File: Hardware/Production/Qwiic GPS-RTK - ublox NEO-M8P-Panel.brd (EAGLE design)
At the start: 95.5 x 94.2 mm, 411 parts, among them J10 U.FL, J13 U.FL, J14 PTH, J17 U.FL, J20 PTH, J23 U.FL, J3 PTH, J7 PTH, U1 NEO-M8P, U2 3.3V, U3 NEO-M8P, U4 3.3V, U5 NEO-M8P, U6 3.3V, U7 NEO-M8P, U8 3.3V

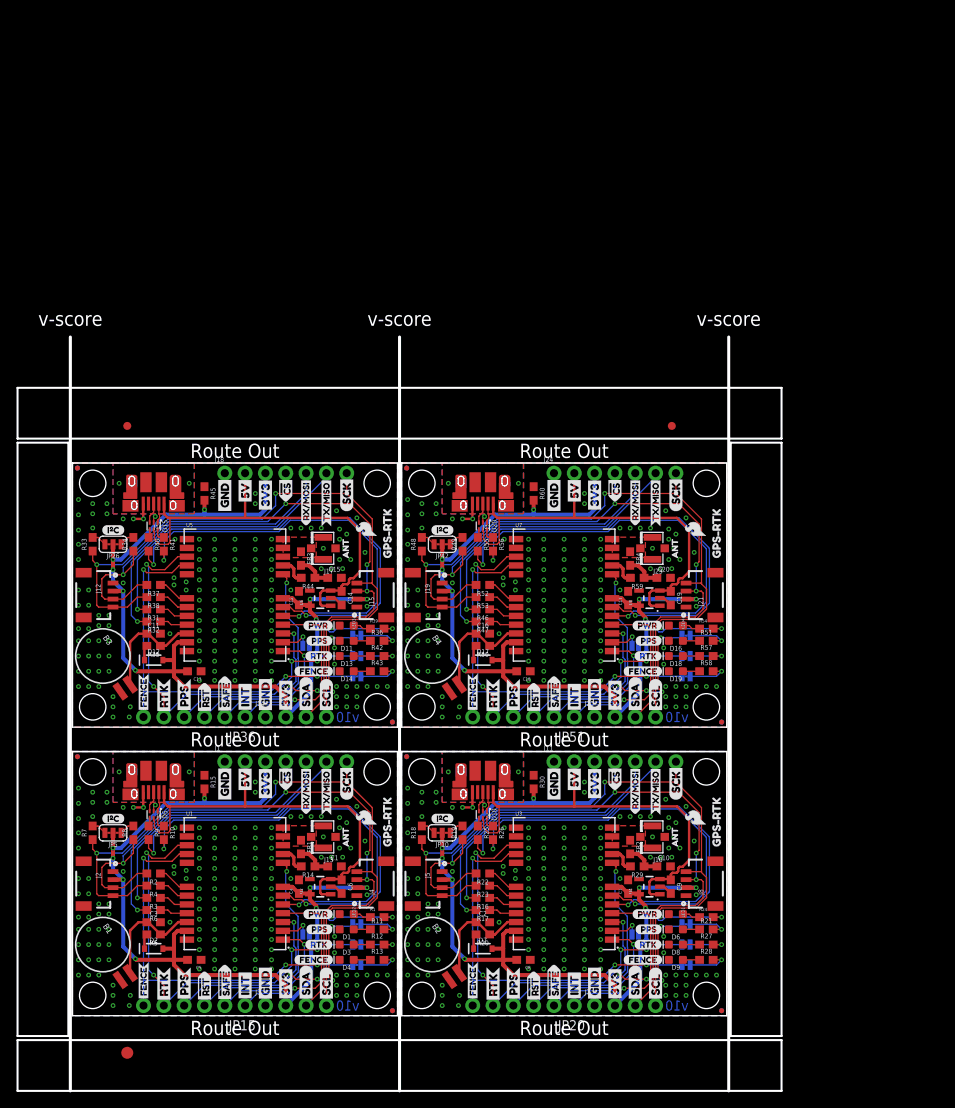
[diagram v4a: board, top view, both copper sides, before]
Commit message: Adds Panel for v20
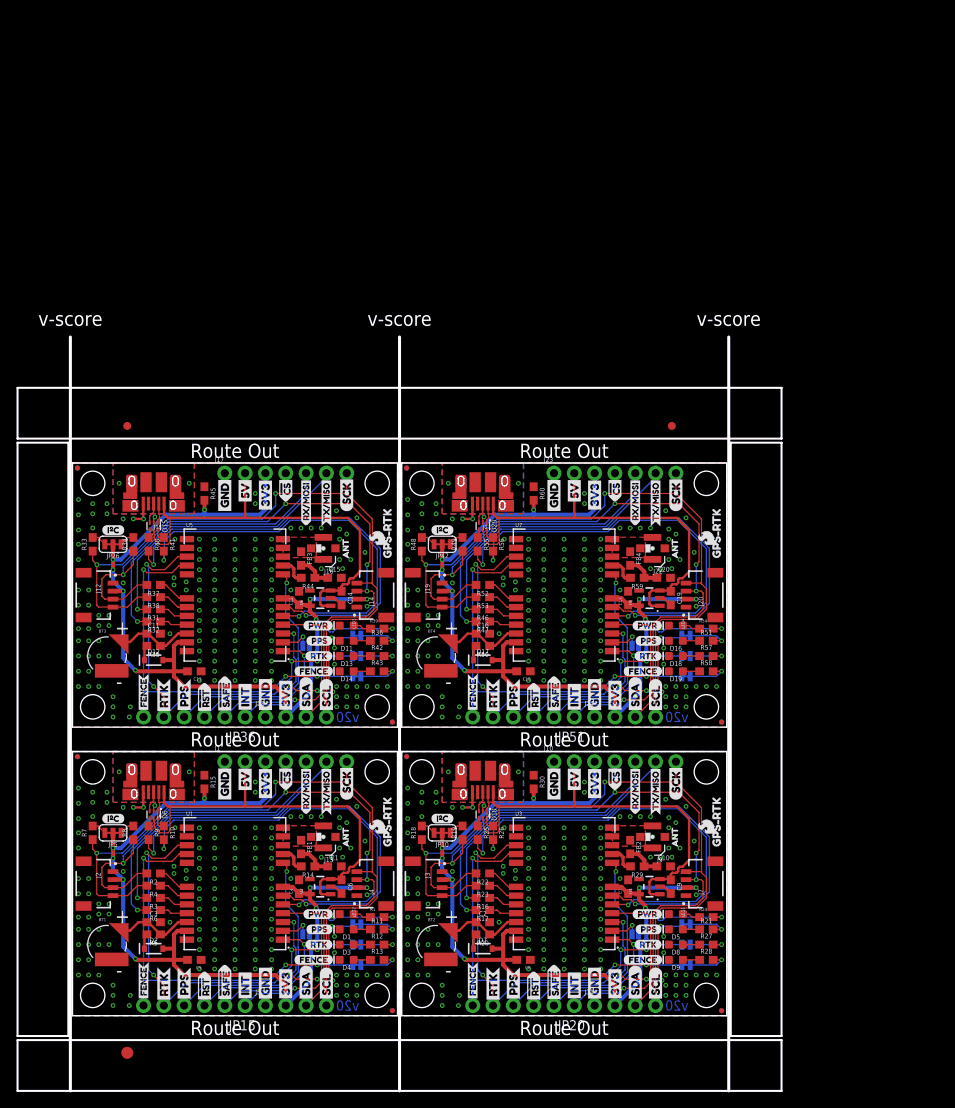
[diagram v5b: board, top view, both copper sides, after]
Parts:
- removed B1, B2, B3, B4: 6.8MM_COIN_CELL, SparkFun-Batteries:BATTCON-6.8MM
- added BT1, BT2, BT3, BT4: ML414H_IV01E_BATTERY, SparkFun-Batteries:ML414H_IV01E
- D10, D15, D20: device funbit:SOT886 -> SparkFun-IC-Power:SOT886
- D5: value PRTR5V0U2F -> Yellow; device funbit:SOT886 -> SparkFun-LED:LED-0603
- D6: value Yellow -> PRTR5V0U2F; device SparkFun-LED:LED-0603 -> SparkFun-IC-Power:SOT886
- J10, J17, J23: value U.FL -> (none); device SparkFun-Connectors:U.FL -> SparkFun-Connectors:1X07_NO_SILK
- J11, J18, J24: device SparkFun-Connectors:1X07_NO_SILK -> SparkFun-Connectors:1X04_NO_SILK
- J12, J19, J2, J4: value (none) -> Qwiic Right Angle; device SparkFun-Connectors:1X04_1MM_RA -> SparkFun-Connectors:JST04_1MM_RA
- J14, J20, J3, J7: value PTH -> Qwiic Right Angle; device SparkX:1X04_NO_SILK -> SparkFun-Connectors:JST04_1MM_RA
- J15, J21, J8: device SparkFun-Connectors:1X04_1MM_RA -> SparkFun-Connectors:USB-MICROB-PTH-MILL
- J16, J22, J9: value (none) -> U.FL; device SparkFun-Connectors:USB-MICROB-PTH-MILL -> SparkFun-Connectors:U.FL
- J5: device SparkFun-Connectors:1X04_1MM_RA -> SparkFun-Connectors:1X04_NO_SILK
- JP1, JP11, JP18, JP19, JP2, JP27, JP3, JP34, JP35, JP43, JP49, JP50: value (none) -> JUMPER-SMT_2_NC_TRACE_SILK
- JP10, JP26, JP42, JP5: value (none) -> JUMPER-SMT_3_2-NC_TRACE_SILK
- JP101, JP14, JP16, JP22, JP23, JP30, JP31, JP32, JP37, JP38, JP41, JP46, JP47, JP6, JP7, JP91: value STAND-OFF -> STAND-OFFTIGHT; device SparkFun:STAND-OFF -> SparkFun-Hardware:STAND-OFF-TIGHT
- JP12, JP13, JP21, JP24, JP25, JP28, JP29, JP39, JP40, JP44, JP45, JP61, JP71, JP8, JP81, JP9: device SparkFun:MICRO-FIDUCIAL -> SparkFun-Aesthetics:FIDUCIAL-MICRO
- JP17, JP33, JP4, JP48: value (none) -> JUMPER-SMT_2_NO_SILK
- U1, U3, U5, U7: device NEO-M8P:NEO-M8P -> SparkFun-GPS:NEO-M8P
- moved D5 66.8 mm to (75.4, 10.8), turned to 180 degrees
- moved D6 66.8 mm to (10.2, 25.1), turned to 270 degrees
- moved J11 30.9 mm to (65.3, 1.27)
- moved J24 30.9 mm to (65.3, 37.3)
- moved J18 30.9 mm to (24.1, 37.3)
- moved J15 27.9 mm to (10.2, 64.0), turned to 180 degrees
- moved J8 27.9 mm to (51.3, 27.9), turned to 180 degrees
- moved J21 27.9 mm to (51.3, 64.0), turned to 180 degrees
- moved J3 26.8 mm to (46.2, 16.5), turned to 270 degrees
- moved J5 26.8 mm to (24.1, 1.27), turned to 0 degrees
- moved J16 21.9 mm to (31.4, 58.4)
- moved J22 21.9 mm to (72.5, 58.4)
- moved J9 21.9 mm to (72.5, 22.4)
- moved J14 19.1 mm to (35.6, 52.6), turned to 90 degrees
- moved J20 19.0 mm to (76.7, 52.6), turned to 90 degrees
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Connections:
- net 3.3V: now also J5.2; no longer J3.2
- net 3.3V1: now also J10.3, J11.2, J3.2; no longer J11.3, J5.2, J8.2
- net 3.3V2: now also J17.3, J18.2; no longer J15.2, J18.3
- net 3.3V3: now also J23.3, J24.2; no longer J21.2, J24.3
- net 5V: now also D6.5; no longer D5.5
- net 5V1: now also J10.2, J8.VBUS; no longer J11.2, J9.VBUS
- net 5V2: now also J15.VBUS, J17.2; no longer J16.VBUS, J18.2
- net 5V3: now also J21.VBUS, J23.2; no longer J22.VBUS, J24.2
- net BACKUP: now also BT1.+; no longer B1.+
- net BACKUP1: now also BT2.+; no longer B2.+
- net BACKUP2: now also BT3.+; no longer B3.+
- net BACKUP3: now also BT4.+; no longer B4.+
- net D+: now also D6.4; no longer D5.4
- net D-: now also D6.6; no longer D5.6
- net GND: now also BT1.-, D6.2, J5.1; no longer B1.-, D5.2, J3.1
- net GND1: now also BT2.-, D5.C, J3.1, J8.GND, J9.1, J9.2; no longer B2.-, D6.C, J10.2, J5.1, J8.1, J9.GND
- net GND2: now also BT3.-, J15.GND, J16.1, J16.2; no longer B3.-, J15.1, J16.GND, J17.2
- net GND3: now also BT4.-, J21.GND, J22.1, J22.2; no longer B4.-, J21.1, J22.GND, J23.2
- net GPS_ANT2: now also J9.FEED; no longer J10.FEED
- net GPS_ANT3: now also J16.FEED; no longer J17.FEED
- net GPS_ANT4: now also J22.FEED; no longer J23.FEED
- net N$16: now also D5.A; no longer D6.A
- net RXI/MOSI1: now also J10.5; no longer J11.5
- net RXI/MOSI2: now also J17.5; no longer J18.5
- net RXI/MOSI3: now also J23.5; no longer J24.5
- net SCL/SCK: now also J5.4; no longer J3.4
- net SCL/SCK1: now also J10.7, J11.4, J3.4; no longer J11.7, J5.4, J8.4
- net SCL/SCK2: now also J17.7, J18.4; no longer J15.4, J18.7
- net SCL/SCK3: now also J23.7, J24.4; no longer J21.4, J24.7
- net SDA/!CS: now also J5.3; no longer J3.3
- net SDA/!CS1: now also J10.4, J11.3, J3.3; no longer J11.4, J5.3, J8.3
- net SDA/!CS2: now also J17.4, J18.3; no longer J15.3, J18.4
- net SDA/!CS3: now also J23.4, J24.3; no longer J21.3, J24.4
- net SHLD1: now also J8.SHIELD, J8.SHIELD10, J8.SHIELD2, J8.SHIELD3, J8.SHIELD4, J8.SHIELD5, J8.SHIELD6, J8.SHIELD7, J8.SHIELD8, J8.SHIELD9; no longer J9.SHIELD, J9.SHIELD10, J9.SHIELD2, J9.SHIELD3, J9.SHIELD4, J9.SHIELD5, J9.SHIELD6, J9.SHIELD7, J9.SHIELD8, J9.SHIELD9
- net SHLD2: now also J15.SHIELD, J15.SHIELD10, J15.SHIELD2, J15.SHIELD3, J15.SHIELD4, J15.SHIELD5, J15.SHIELD6, J15.SHIELD7, J15.SHIELD8, J15.SHIELD9; no longer J16.SHIELD, J16.SHIELD10, J16.SHIELD2, J16.SHIELD3, J16.SHIELD4, J16.SHIELD5, J16.SHIELD6, J16.SHIELD7, J16.SHIELD8, J16.SHIELD9
- net SHLD3: now also J21.SHIELD, J21.SHIELD10, J21.SHIELD2, J21.SHIELD3, J21.SHIELD4, J21.SHIELD5, J21.SHIELD6, J21.SHIELD7, J21.SHIELD8, J21.SHIELD9; no longer J22.SHIELD, J22.SHIELD10, J22.SHIELD2, J22.SHIELD3, J22.SHIELD4, J22.SHIELD5, J22.SHIELD6, J22.SHIELD7, J22.SHIELD8, J22.SHIELD9
- net TXO/MISO1: now also J10.6; no longer J11.6
- net TXO/MISO2: now also J17.6; no longer J18.6
- net TXO/MISO3: now also J23.6; no longer J24.6
- net USB_D+: now also D6.3; no longer D5.3
- net USB_D+1: now also J8.D+; no longer J9.D+
- net USB_D+2: now also J15.D+; no longer J16.D+
- net USB_D+3: now also J21.D+; no longer J22.D+
- net USB_D-: now also D6.1; no longer D5.1
- net USB_D-1: now also J8.D-; no longer J9.D-
- net USB_D-2: now also J15.D-; no longer J16.D-
- net USB_D-3: now also J21.D-; no longer J22.D-
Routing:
- net BACKUP1: track 14.1 -> 9.80 mm
- net BACKUP: track 14.1 -> 9.80 mm
- net BACKUP2: track 14.1 -> 9.80 mm
- net BACKUP3: track 14.1 -> 9.80 mm
- net GND1: track 5.71 -> 5.61 mm, vias 161 -> 158
- net GND: track 5.71 -> 5.61 mm, vias 161 -> 158
- net GND3: track 5.71 -> 5.61 mm, vias 161 -> 158
- net GND2: track 5.71 -> 5.61 mm, vias 161 -> 158
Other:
- board text added: "+"
- board text added: "-"
- board text added: "v20"
- board text removed: "v10"

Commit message: Repanelizes for a larger panel 2x3 instead of 2x2
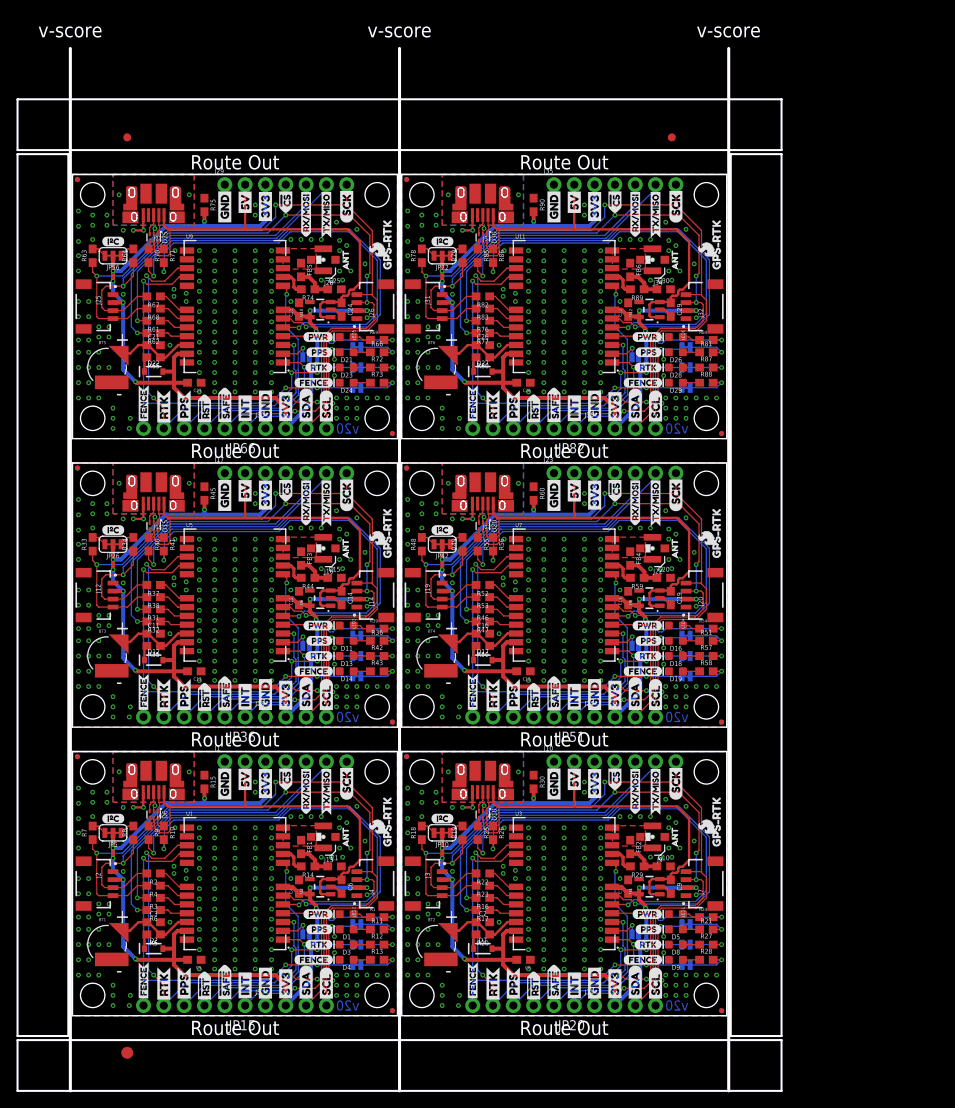
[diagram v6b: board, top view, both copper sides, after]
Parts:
- added BT5, BT6: ML414H_IV01E_BATTERY, SparkFun-Batteries:ML414H_IV01E
- added C21, C22, C24, C26, C27, C29: 1.0uF, SparkFun-Capacitors:0603
- added C23, C28: 0.1uF, SparkFun-Capacitors:0603
- added C25, C30: 47pF, SparkFun-Capacitors:0603
- added D21, D26: Yellow, SparkFun-LED:LED-0603
- added D22, D27: 0.5A/40V/420mV, SparkFun-DiscreteSemi:SOD-323
- added D23, D28: GREEN, SparkFun-LED:LED-0603
- added D24, D29: BLUE, SparkFun-LED:LED-0603
- added D25, D30: PRTR5V0U2F, SparkFun-IC-Power:SOT886
- added FB5, FB6: 30Ω/1.8A, SparkFun-Coils:0603
- added J25, J26, J31, J32: Qwiic Right Angle, SparkFun-Connectors:JST04_1MM_RA
- added J27, J33: (no value), SparkFun-Connectors:USB-MICROB-PTH-MILL
- added J28, J34: U.FL, SparkFun-Connectors:U.FL
- added J29, J35: (no value), SparkFun-Connectors:1X07_NO_SILK
- added J30, J36: (no value), SparkFun-Connectors:1X04_NO_SILK
- added JP52, JP53, JP60, JP62, JP67, JP68, JP76, JP77: STAND-OFFTIGHT, SparkFun-Hardware:STAND-OFF-TIGHT
- added JP54, JP55, JP58, JP59, JP69, JP70, JP74, JP75: FIDUCIALUFIDUCIAL, SparkFun-Aesthetics:FIDUCIAL-MICRO
- added JP56, JP72: JUMPER-SMT_3_2-NC_TRACE_SILK, SparkFun-Jumpers:SMT-JUMPER_3_2-NC_TRACE_SILK
- added JP57, JP64, JP65, JP73, JP79, JP80: JUMPER-SMT_2_NC_TRACE_SILK, SparkFun-Jumpers:SMT-JUMPER_2_NC_TRACE_SILK
- added JP63, JP78: JUMPER-SMT_2_NO_SILK, SparkFun-Jumpers:SMT-JUMPER_2_NO_SILK
- added JP66, JP82: (no value), SparkFun-Connectors:1X06_NO_SILK
- added LED5, LED6: RED, SparkFun-LED:LED-0603
- added LOGO10, LOGO12: SFE_LOGO_NAME_FLAME.1_INCH, SparkFun-Aesthetics:SFE_LOGO_NAME_FLAME_.1
- added LOGO11, LOGO9: OSHW-LOGOMINI, SparkFun-Aesthetics:OSHW-LOGO-MINI
- added R61, R62, R67, R68, R76, R77, R82, R83: 33, SparkFun-Resistors:0603
- added R63, R64, R78, R79: 2.2k, SparkFun-Resistors:0603
- added R65, R66, R69, R72, R73, R80, R81, R84, R87, R88: 1k, SparkFun-Resistors:0603
- added R70, R71, R85, R86: 27, SparkFun-Resistors:0603
- added R74, R89: 10, SparkFun-Resistors:0603
- added R75, R90: 100k, SparkFun-Resistors:0603
- added U$201, U$203, U$251, U$253: (no value), Labels:SDA-[)
- added U$202, U$204, U$252, U$254: (no value), Labels:SCL-[)
- added U$205, U$206, U$228, U$229, U$255, U$256, U$278, U$279: (no value), Labels:3V3-04
- added U$207, U$208, U$230, U$231, U$257, U$258, U$280, U$281: (no value), Labels:GND-04
- added U$209, U$259: (no value), Labels:I_SUPER2_C-()-03
- added U$210, U$211, U$260, U$261: (no value), buzzard_labels (5):INT8
- added U$212, U$262: (no value), buzzard_labels (5):U#BLOX3
- added U$213, U$263: (no value), Labels:QWIIC-LOGO-MEDIUM
- added U$214, U$215, U$264, U$265: (no value), buzzard_labels (7):#RST3
- added U$216, U$217, U$266, U$267: (no value), buzzard_labels (7):#SAFE1
- added U$218, U$219, U$268, U$269: (no value), buzzard_labels (7):PPS5
- added U$220, U$270: (no value), buzzard_labels (33):PPS0
- added U$221, U$271: (no value), buzzard_labels:FENCE2
- added U$222, U$272: (no value), buzzard_labels:JP20
- added U$223, U$273: (no value), buzzard_labels:RTK1
- added U$224, U$225, U$274, U$275: (no value), buzzard_labels (1):FENCE0
- added U$226, U$227, U$276, U$277: (no value), buzzard_labels (1):RTK1
- added U$232, U$282: (no value), buzzard_labels (3):GPS#RTK0
- added U$233, U$283: (no value), buzzard_labels (5):JP10
- added U$234, U$284: (no value), buzzard_labels (5):JP32
- added U$235, U$285: (no value), buzzard_labels (6):DSEL0
- added U$236, U$286: (no value), buzzard_labels (7):NEO#M8P3
- added U$237, U$287: (no value), buzzard_labels (8):GPS#RTK1
- added U$238, U$288: (no value), buzzard_labels (9):ANT0
- added U$239, U$289: (no value), Labels:PWR-()-03
- added U$240, U$241, U$290, U$291: (no value), Labels:5V
- added U$242, U$243, U$292, U$293: (no value), Labels:CS#-<]
- added U$244, U$245, U$294, U$295: (no value), Labels:SCK-(]-04
- added U$246, U$296: (no value), SparkFun-Aesthetics:SFE_LOGO_FLAME_.1
- added U$247, U$297: (no value), buzzard_labels (36):RX#MOSI2
- added U$248, U$298: (no value), buzzard_labels (36):RX#MOSI3
- added U$249, U$299: (no value), buzzard_labels (36):TX#MISO0
- added U$250, U$300: (no value), buzzard_labels (36):TX#MISO1
- added U10, U12: 3.3V, SparkFun-IC-Power:SOT23-5
- added U11, U9: NEO-M8P, SparkFun-GPS:NEO-M8P
- moved E$1 36.1 mm to (6.86, 109.8)
- moved E$2 36.1 mm to (74.9, 109.8)
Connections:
- new net !RESET4: JP66.3, U9.8
- new net !RESET5: JP82.3, U11.8
- new net !SAFE4: JP66.2, U9.1
- new net !SAFE5: JP82.2, U11.1
- new net 3.3V4: C22.1, C23.2, D22.A, J25.2, J26.2, J29.3, J30.2, JP56.2, R69.2, R75.2, U10.5, U9.23, U9.7
- new net 3.3V5: C27.1, C28.2, D27.A, J31.2, J32.2, J35.3, J36.2, JP72.2, R84.2, R90.2, U11.23, U11.7, U12.5
- new net 5V4: C24.1, D25.5, J27.VBUS, J29.2, U10.1, U10.3
- new net 5V5: C29.1, D30.5, J33.VBUS, J35.2, U12.1, U12.3
- new net ANT_VCC4: C25.1, FB5.2, R74.1
- new net ANT_VCC5: C30.1, FB6.2, R89.1
- new net BACKUP4: BT5.+, C21.1, R65.1, U9.22
- new net BACKUP5: BT6.+, C26.1, R80.1, U11.22
- new net D+4: D25.4, R70.1
- new net D+5: D30.4, R85.1
- new net D-4: D25.6, R71.1
- new net D-5: D30.6, R86.1
- new net D_SEL4: JP63.2, U9.2
- new net D_SEL5: JP78.2, U11.2
- new net FENCE_STAT4: JP65.2, JP66.6, U9.16
- new net FENCE_STAT5: JP80.2, JP82.6, U11.16
- new net GND4: BT5.-, C21.2, C22.2, C23.1, C24.2, C25.2, D21.C, D23.C, D24.C, D25.2, J25.1, J26.1, J27.GND, J28.1, J28.2, J29.1, J30.1, JP63.1, LED5.C, R75.1, U10.2, U9.10, U9.12, U9.13, U9.24
- new net GND5: BT6.-, C26.2, C27.2, C28.1, C29.2, C30.2, D26.C, D28.C, D29.C, D30.2, J31.1, J32.1, J33.GND, J34.1, J34.2, J35.1, J36.1, JP78.1, LED6.C, R90.1, U11.10, U11.12, U11.13, U11.24, U12.2
- new net GPS_ANT5: FB5.1, J28.FEED, U9.11
- new net GPS_ANT6: FB6.1, J34.FEED, U11.11
- new net INT4: JP66.1, U9.4
- new net INT5: JP82.1, U11.4
- new net N$53: JP56.1, R64.2
- new net N$54: JP56.3, R63.2
- new net N$55: D21.A, R66.1
- new net N$56: JP57.1, R66.2
- new net N$57: D22.C, R65.2
- new net N$58: LED5.A, R69.1
- new net N$59: R70.2, U9.6
- new net N$60: R71.2, U9.5
- new net N$61: D23.A, R72.1
- new net N$62: JP64.1, R72.2
- new net N$63: D24.A, R73.1
- new net N$64: JP65.1, R73.2
- new net N$65: R74.2, U9.9
- new net N$66: JP72.1, R79.2
- new net N$67: JP72.3, R78.2
- new net N$68: D26.A, R81.1
- new net N$69: JP73.1, R81.2
- new net N$70: D27.C, R80.2
- new net N$71: LED6.A, R84.1
- new net N$72: R85.2, U11.6
- new net N$73: R86.2, U11.5
- new net N$74: D28.A, R87.1
- new net N$75: JP79.1, R87.2
- new net N$76: D29.A, R88.1
- new net N$77: JP80.1, R88.2
- new net N$78: R89.2, U11.9
- new net PPS4: JP57.2, JP66.4, U9.3
- new net PPS5: JP73.2, JP82.4, U11.3
- new net RTK_STAT4: JP64.2, JP66.5, U9.15
- new net RTK_STAT5: JP79.2, JP82.5, U11.15
- new net RXI/MOSI4: J29.5, R62.2
- new net RXI/MOSI5: J35.5, R77.2
- new net RXLV4: R62.1, U9.21
- new net RXLV5: R77.1, U11.21
- new net SCL/SCK4: J25.4, J26.4, J29.7, J30.4, R63.1, R68.2
- new net SCL/SCK5: J31.4, J32.4, J35.7, J36.4, R78.1, R83.2
- new net SCL_LV4: R68.1, U9.19
- new net SCL_LV5: R83.1, U11.19
- new net SDA/!CS4: J25.3, J26.3, J29.4, J30.3, R64.1, R67.2
- new net SDA/!CS5: J31.3, J32.3, J35.4, J36.3, R79.1, R82.2
- new net SDA_LV4: R67.1, U9.18
- new net SDA_LV5: R82.1, U11.18
- new net SHLD4: J27.SHIELD, J27.SHIELD10, J27.SHIELD2, J27.SHIELD3, J27.SHIELD4, J27.SHIELD5, J27.SHIELD6, J27.SHIELD7, J27.SHIELD8, J27.SHIELD9
- new net SHLD5: J33.SHIELD, J33.SHIELD10, J33.SHIELD2, J33.SHIELD3, J33.SHIELD4, J33.SHIELD5, J33.SHIELD6, J33.SHIELD7, J33.SHIELD8, J33.SHIELD9
- new net TXLV4: R61.1, U9.20
- new net TXLV5: R76.1, U11.20
- new net TXO/MISO4: J29.6, R61.2
- new net TXO/MISO5: J35.6, R76.2
- new net USB_D+4: D25.3, J27.D+
- new net USB_D+5: D30.3, J33.D+
- new net USB_D-4: D25.1, J27.D-
- new net USB_D-5: D30.1, J33.D-
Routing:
- net 3.3V4: track 0.00 -> 118.9 mm, vias 0 -> 9
- net 3.3V5: track 0.00 -> 118.9 mm, vias 0 -> 9
- net SCL/SCK5: track 0.00 -> 88.9 mm, vias 0 -> 2
- net SCL/SCK4: track 0.00 -> 88.9 mm, vias 0 -> 2
- net SDA/!CS5: track 0.00 -> 87.3 mm, vias 0 -> 4
- net SDA/!CS4: track 0.00 -> 87.3 mm, vias 0 -> 4
- net N$59: track 0.00 -> 55.6 mm, vias 0 -> 2
- net N$72: track 0.00 -> 55.6 mm, vias 0 -> 2
- net RTK_STAT5: track 0.00 -> 53.9 mm, vias 0 -> 4
- net RTK_STAT4: track 0.00 -> 53.9 mm, vias 0 -> 4
- net 5V5: track 0.00 -> 53.5 mm
- net 5V4: track 0.00 -> 53.5 mm
- net N$60: track 0.00 -> 52.2 mm, vias 0 -> 2
- net N$73: track 0.00 -> 52.2 mm, vias 0 -> 2
- net FENCE_STAT5: track 0.00 -> 51.4 mm, vias 0 -> 3
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- added copper zone on layer 1, net GND4
- added copper zone on layer 16, net GND4
- added copper zone on layer 1, net GND5
- added copper zone on layer 16, net GND5
- added copper zone on layer 1, net GPS_ANT5
- added copper zone on layer 1, net GPS_ANT6
- added copper zone on layer 1, net SHLD4
- added copper zone on layer 16, net SHLD4
- added copper zone on layer 1, net SHLD5
- added copper zone on layer 16, net SHLD5
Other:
- board size 95.5 x 94.2 mm -> 95.5 x 130.3 mm
